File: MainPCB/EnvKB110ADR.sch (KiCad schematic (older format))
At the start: 246 parts, among them U1 MCP23017, U2 Pico

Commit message: setup some board bits
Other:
- moved on the sheet: D_0, D_1, D_10, D_100, D_101, D_102, D_103, D_104, D_105, D_106, D_107, D_108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

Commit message: Started work on swapping RPI pico for STM32F411CEU6
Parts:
- removed D_0, D_1, D_10, D_11, D_2, D_3, D_4, D_5, D_6, D_7, D_8, D_9: SOD-123, Diode_SMD:D_SOD-123, symbol Device:D_Small
- removed H7: MountingHole, MountingHole:MountingHole_2.2mm_M2, symbol Mechanical:MountingHole
- removed K_0, K_1, K_10, K_11, K_2, K_3, K_4, K_5, K_6, K_7, K_8, K_9: KEYSW, MX_Only:MXOnly-1U-Hotswap, symbol MX_Alps_Hybrid:MX-NoLED
- removed U1: MCP23017, Package_SO:SOIC-28W_7.5x17.9mm_P1.27mm, symbol Interface_Expansion:MCP23017_SO
- removed U2: Pico, MCU_RaspberryPi_and_Boards:RPi_Pico_SMD_TH, symbol MCU_RaspberryPi_and_Boards:Pico
- added C1, C2, C3, C4: 100nf capacitor, Capacitor_SMD:C_0402_1005Metric, symbol Device:C_Small
- added R1: 1.5K, Resistor_SMD:R_0402_1005Metric, symbol Device:R_Small
- added R2, R5: 5.1K 0402, Resistor_SMD:R_0402_1005Metric, symbol Device:R_Small
- added R3, R4: 22ohm, Resistor_SMD:R_0402_1005Metric, symbol Device:R_Small
- added U1: XC6206PxxxMR, Package_TO_SOT_SMD:SOT-23, symbol Regulator_Linear:XC6206PxxxMR
- added U2: STM32F411CEUx, Package_DFN_QFN:QFN-48-1EP_7x7mm_P0.5mm_EP5.6x5.6mm, symbol MCU_ST_STM32F4:STM32F411CEUx
- added USB1: HRO-TYPE-C-31-M-12, Type-C:HRO-TYPE-C-31-M-12-Assembly, symbol Type-C:HRO-TYPE-C-31-M-12
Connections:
- net labels added: D+, D-, PA11, PA12, VBUS
- net labels removed: SCL, SDA, col18, row0
- wire segments 468 -> 445
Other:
- note added: "these capacitors should all be placed\n near the power pin of the STM32"
- note added: "unsure what this pullup resistor is for\nbut its used in some MCU boards so lets copy it"

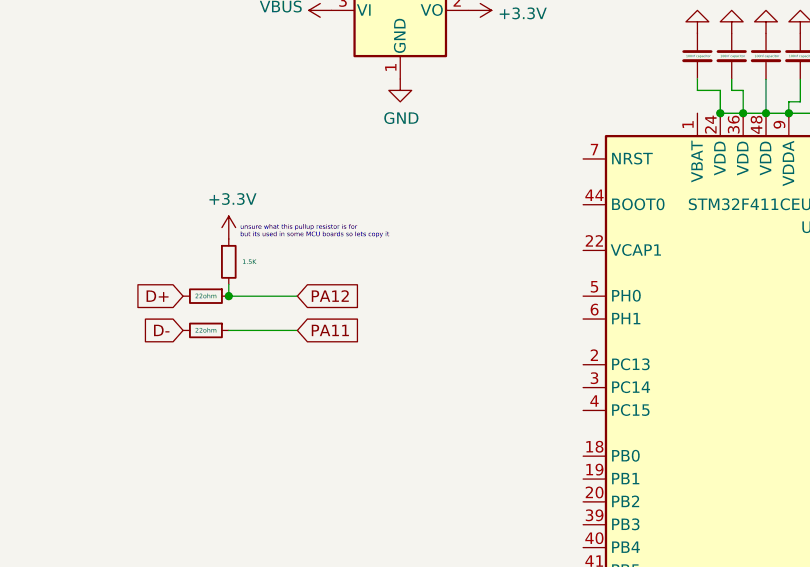
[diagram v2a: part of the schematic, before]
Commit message: added some notes in the schematic
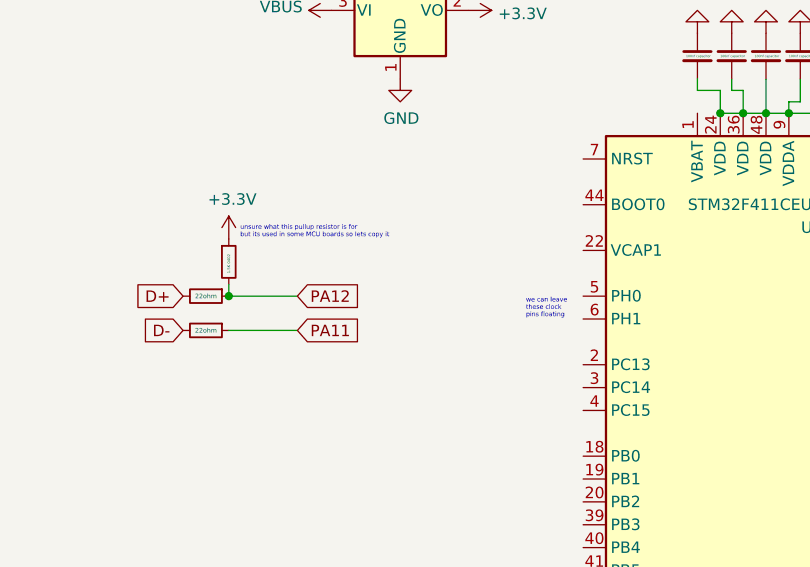
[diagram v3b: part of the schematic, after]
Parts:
- R1: value 1.5K -> 1.5K 0402
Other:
- note added: "we can leave \nthese clock\npins floating"
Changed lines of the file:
@@
 P 11150 10500
 F 0 "R1" H 11209 10546 50  0001 L CNN
-F 1 "1.5K" H 11209 10500 20  0000 L CNN
+F 1 "1.5K 0402" V 11150 10450 12  0000 L CNN
 F 2 "Resistor_SMD:R_0402_1005Metric" H 11150 10500 50  0001 C CNN
 F 3 "~" H 11150 10500 50  0001 C CNN
@@
 	1    0    0    -1
 $EndComp
+Text Notes 12450 10750 0    20   ~ 0
+we can leave \nthese clock\npins floating
 $EndSCHEMATC

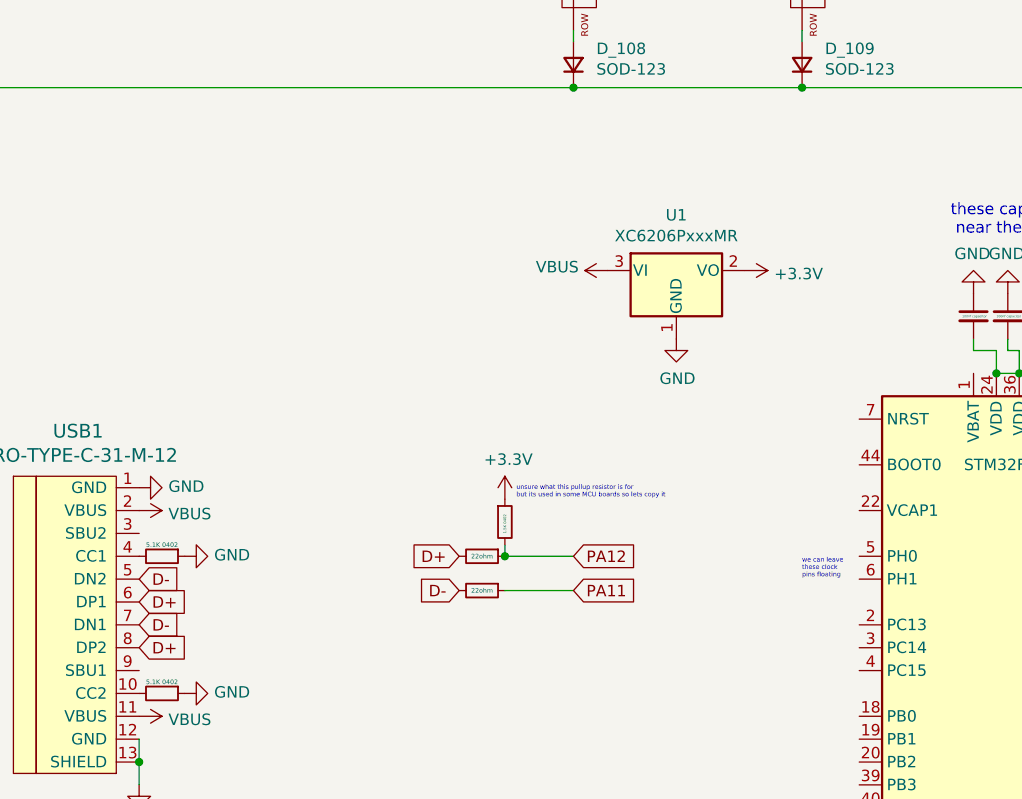
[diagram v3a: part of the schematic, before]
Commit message: hopefully correct implementation of a 8mhz oscilator
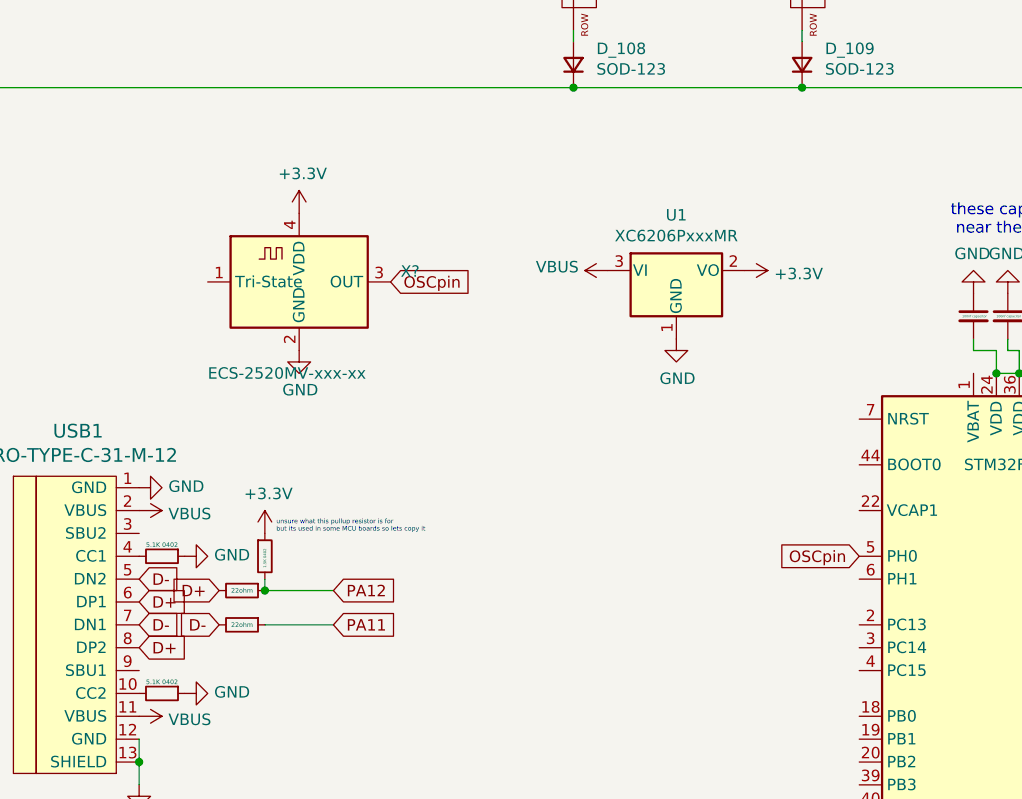
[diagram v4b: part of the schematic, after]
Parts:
- added X?: ECS-2520MV-xxx-xx, Oscillator:Oscillator_SMD_ECS_2520MV-xxx-xx-4Pin_2.5x2.0mm, symbol Oscillator:ECS-2520MV-xxx-xx
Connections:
- net +3V3: now also X?.4 (VDD)
- net GND: now also X?.2 (GND)
- net OSCpin: now reaches U2.5 (PH0)
- net OSCpin: now also X?.3 (OUT)
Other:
- note removed: "we can leave \nthese clock\npins floating"
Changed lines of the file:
@@
 Text GLabel 9550 11050 2    50   Input ~ 0
 D+
-Text GLabel 10950 10650 0    50   Input ~ 0
+Text GLabel 9900 10800 0    50   Input ~ 0
 D+
-Text GLabel 10950 10800 0    50   Input ~ 0
+Text GLabel 9900 10950 0    50   Input ~ 0
 D-
 $Comp
 L Device:R_Small R3
 U 1 1 6149657B
-P 11050 10650
-F 0 "R3" V 10854 10650 50  0001 C CNN
-F 1 "22ohm" V 11050 10650 20  0000 C CNN
-F 2 "Resistor_SMD:R_0402_1005Metric" H 11050 10650 50  0001 C CNN
-F 3 "~" H 11050 10650 50  0001 C CNN
-	1    11050 10650
+P 10000 10800
+F 0 "R3" V 9804 10800 50  0001 C CNN
+F 1 "22ohm" V 10000 10800 20  0000 C CNN
+F 2 "Resistor_SMD:R_0402_1005Metric" H 10000 10800 50  0001 C CNN
+F 3 "~" H 10000 10800 50  0001 C CNN
+	1    10000 10800
 	0    1    1    0
 $EndComp
@@
 L Device:R_Small R4
 U 1 1 614993EB
-P 11050 10800
-F 0 "R4" V 10854 10800 50  0001 C CNN
-F 1 "22ohm" V 11050 10800 20  0000 C CNN
-F 2 "Resistor_SMD:R_0402_1005Metric" H 11050 10800 50  0001 C CNN
-F 3 "~" H 11050 10800 50  0001 C CNN
-	1    11050 10800
+P 10000 10950
+F 0 "R4" V 9804 10950 50  0001 C CNN
+F 1 "22ohm" V 10000 10950 20  0000 C CNN
+F 2 "Resistor_SMD:R_0402_1005Metric" H 10000 10950 50  0001 C CNN
+F 3 "~" H 10000 10950 50  0001 C CNN
+	1    10000 10950
 	0    1    1    0
 $EndComp
@@
 L power:+3.3V #PWR0110
 U 1 1 6149994E
-P 11150 10400
-F 0 "#PWR0110" H 11150 10250 50  0001 C CNN
-F 1 "+3.3V" H 11165 10573 50  0000 C CNN
-F 2 "" H 11150 10400 50  0001 C CNN
-F 3 "" H 11150 10400 50  0001 C CNN
-	1    11150 10400
+P 10100 10550
+F 0 "#PWR0110" H 10100 10400 50  0001 C CNN
+F 1 "+3.3V" H 10115 10723 50  0000 C CNN
+F 2 "" H 10100 10550 50  0001 C CNN
+F 3 "" H 10100 10550 50  0001 C CNN
+	1    10100 10550
 	1    0    0    -1
 $EndComp
@@
 L Device:R_Small R1
 U 1 1 6149AD81
-P 11150 10500
-F 0 "R1" H 11209 10546 50  0001 L CNN
-F 1 "1.5K 0402" V 11150 10450 12  0000 L CNN
-F 2 "Resistor_SMD:R_0402_1005Metric" H 11150 10500 50  0001 C CNN
-F 3 "~" H 11150 10500 50  0001 C CNN
-	1    11150 10500
+P 10100 10650
+F 0 "R1" H 10159 10696 50  0001 L CNN
+F 1 "1.5K 0402" V 10100 10600 12  0000 L CNN
+F 2 "Resistor_SMD:R_0402_1005Metric" H 10100 10650 50  0001 C CNN
+F 3 "~" H 10100 10650 50  0001 C CNN
+	1    10100 10650
 	1    0    0    -1
 $EndComp
 Wire Wire Line
-	11150 10600 11150 10650
+	10100 10750 10100 10800
 Wire Wire Line
-	11150 10650 11450 10650
-Connection ~ 11150 10650
+	10100 10800 10400 10800
+Connection ~ 10100 10800
 Wire Wire Line
-	11150 10800 11450 10800
-Text GLabel 11450 10650 2    50   Input ~ 0
+	10100 10950 10400 10950
+Text GLabel 10400 10800 2    50   Input ~ 0
 PA12
-Text GLabel 11450 10800 2    50   Input ~ 0
+Text GLabel 10400 10950 2    50   Input ~ 0
 PA11
 Text GLabel 14000 12450 2    50   Input ~ 0
@@
 Text GLabel 14000 12350 2    50   Input ~ 0
 PA11
-Text Notes 11200 10400 0    20   ~ 0
+Text Notes 10150 10550 0    20   ~ 0
 unsure what this pullup resistor is for\nbut its used in some MCU boards so lets copy it
 $Comp
@@
 	1    0    0    -1
 $EndComp
-Text Notes 12450 10750 0    20   ~ 0
-we can leave \nthese clock\npins floating
+$Comp
+L Oscillator:ECS-2520MV-xxx-xx X?
+U 1 1 60E5B405
+P 10250 9450
+F 0 "X?" H 10694 9496 50  0000 L CNN
+F 1 "ECS-2520MV-xxx-xx" H 9850 9050 50  0000 L CNN
+F 2 "Oscillator:Oscillator_SMD_ECS_2520MV-xxx-xx-4Pin_2.5x2.0mm" H 10700 9100 50  0001 C CNN
+F 3 "https://www.ecsxtal.com/store/pdf/ECS-2520MV.pdf" H 10075 9575 50  0001 C CNN
+	1    10250 9450
+	1    0    0    -1
+$EndComp
+Text GLabel 10650 9450 2    50   Input ~ 0
+OSCpin
+Text GLabel 12700 10650 0    50   Input ~ 0
+OSCpin
+$Comp
+L power:+3.3V #PWR?
+U 1 1 60E980B3
+P 10250 9150
+F 0 "#PWR?" H 10250 9000 50  0001 C CNN
+F 1 "+3.3V" H 10265 9323 50  0000 C CNN
+F 2 "" H 10250 9150 50  0001 C CNN
+F 3 "" H 10250 9150 50  0001 C CNN
+	1    10250 9150
+	1    0    0    -1
+$EndComp
+$Comp
+L power:GND #PWR?
+U 1 1 60E99EB6
+P 10250 9750
+F 0 "#PWR?" H 10250 9500 50  0001 C CNN
+F 1 "GND" H 10255 9577 50  0000 C CNN
+F 2 "" H 10250 9750 50  0001 C CNN
+F 3 "" H 10250 9750 50  0001 C CNN
+	1    10250 9750
+	1    0    0    -1
+$EndComp
 $EndSCHEMATC

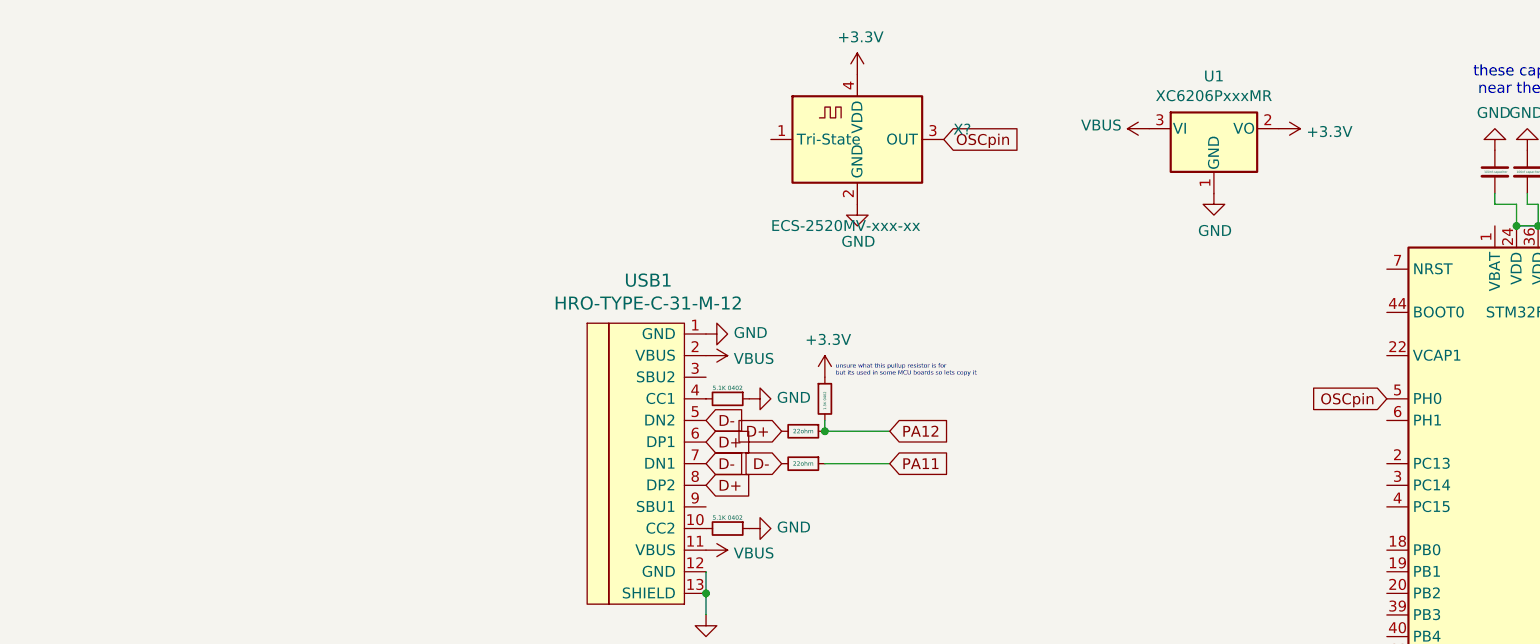
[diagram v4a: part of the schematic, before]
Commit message: added boot and reset switches
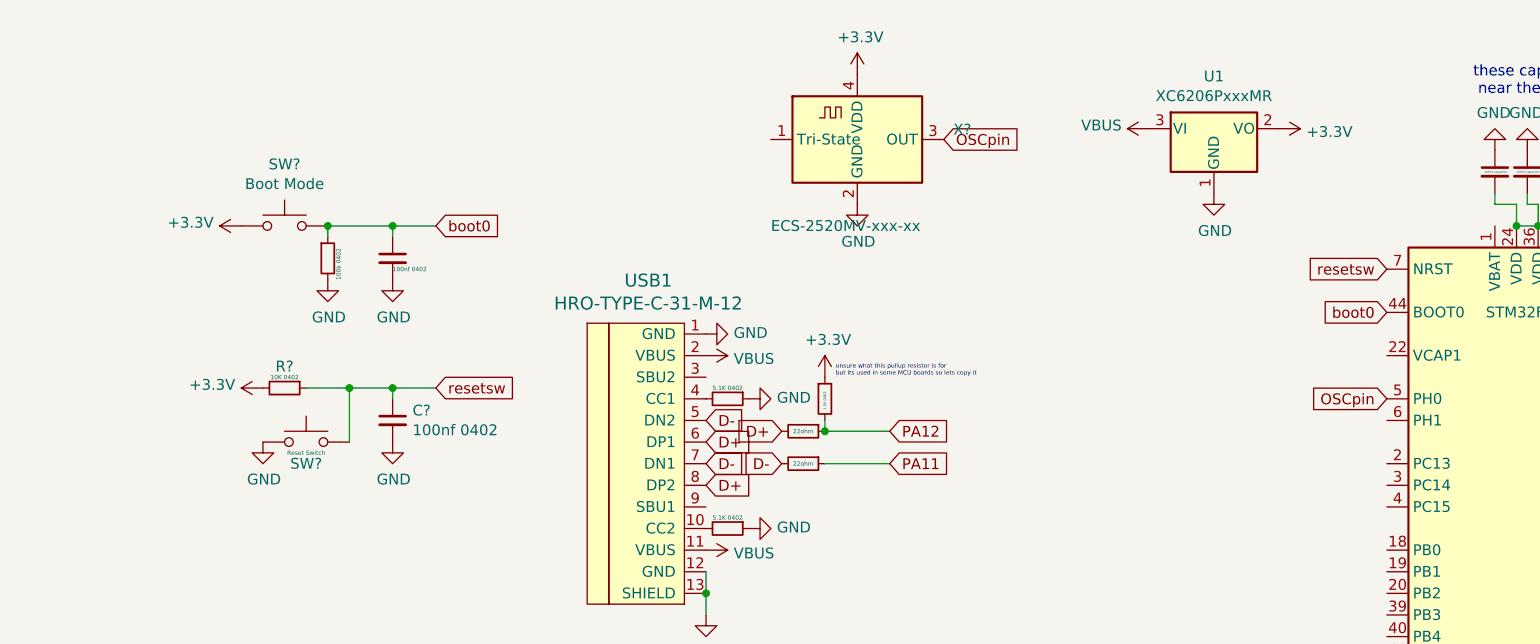
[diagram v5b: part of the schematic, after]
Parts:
- added C? (x2): 100nf 0402, Capacitor_SMD:C_0402_1005Metric, symbol Device:C_Small
- added R?: 100k 0402, Resistor_SMD:R_0402_1005Metric, symbol Device:R_Small
- added R?: 10K 0402, Resistor_SMD:R_0402_1005Metric, symbol Device:R_Small
- added SW?: Boot Mode, Button_Switch_SMD:SW_DIP_SPSTx01_Slide_6.7x4.1mm_W6.73mm_P2.54mm_LowProfile_JPin, symbol Switch:SW_Push
- added SW?: Reset Switch, Button_Switch_SMD:SW_DIP_SPSTx01_Slide_6.7x4.1mm_W6.73mm_P2.54mm_LowProfile_JPin, symbol Switch:SW_Push
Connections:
- net +3V3: now also R?.2, SW?.1
- net GND: now also C?.2, C?.2, R?.2, SW?.1
- net boot0: now reaches U2.44 (BOOT0)
- net boot0: now also C?.1, R?.1, SW?.2
- net resetsw: now reaches U2.7 (NRST)
- net resetsw: now also C?.1, R?.1, SW?.2
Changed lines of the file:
@@
 	1    0    0    -1
 $EndComp
+Text GLabel 12700 10250 0    50   Input ~ 0
+boot0
+Text GLabel 8300 9850 2    50   Input ~ 0
+boot0
+$Comp
+L power:GND #PWR?
+U 1 1 60E6F770
+P 8100 10100
+F 0 "#PWR?" H 8100 9850 50  0001 C CNN
+F 1 "GND" H 8105 9927 50  0000 C CNN
+F 2 "" H 8100 10100 50  0001 C CNN
+F 3 "" H 8100 10100 50  0001 C CNN
+	1    8100 10100
+	1    0    0    -1
+$EndComp
+$Comp
+L power:GND #PWR?
+U 1 1 60E6FF51
+P 7800 10100
+F 0 "#PWR?" H 7800 9850 50  0001 C CNN
+F 1 "GND" H 7805 9927 50  0000 C CNN
+F 2 "" H 7800 10100 50  0001 C CNN
+F 3 "" H 7800 10100 50  0001 C CNN
+	1    7800 10100
+	1    0    0    -1
+$EndComp
+$Comp
+L Device:R_Small R?
+U 1 1 60E71B24
+P 7800 10000
+F 0 "R?" H 7859 10046 50  0001 L CNN
+F 1 "100k 0402" V 7850 9900 20  0000 L CNN
+F 2 "Resistor_SMD:R_0402_1005Metric" H 7800 10000 50  0001 C CNN
+F 3 "~" H 7800 10000 50  0001 C CNN
+	1    7800 10000
+	1    0    0    -1
+$EndComp
+$Comp
+L Device:C_Small C?
+U 1 1 60E73582
+P 8100 10000
+F 0 "C?" H 8192 10046 50  0001 L CNN
+F 1 "100nf 0402" H 8100 9950 20  0000 L CNN
+F 2 "Capacitor_SMD:C_0402_1005Metric" H 8100 10000 50  0001 C CNN
+F 3 "~" H 8100 10000 50  0001 C CNN
+	1    8100 10000
+	1    0    0    -1
+$EndComp
+Wire Wire Line
+	8300 9850 8100 9850
+Wire Wire Line
+	8100 9850 8100 9900
+Wire Wire Line
+	8100 9850 7800 9850
+Wire Wire Line
+	7800 9850 7800 9900
+Connection ~ 8100 9850
+$Comp
+L Switch:SW_Push SW?
+U 1 1 60EE310E
+P 7600 9850
+F 0 "SW?" H 7600 10135 50  0000 C CNN
+F 1 "Boot Mode" H 7600 10044 50  0000 C CNN
+F 2 "Button_Switch_SMD:SW_DIP_SPSTx01_Slide_6.7x4.1mm_W6.73mm_P2.54mm_LowProfile_JPin" H 7600 10043 50  0001 C CNN
+F 3 "~" H 7600 10050 50  0001 C CNN
+	1    7600 9850
+	1    0    0    -1
+$EndComp
+Connection ~ 7800 9850
+$Comp
+L power:+3.3V #PWR?
+U 1 1 60EE5DF1
+P 7400 9850
+F 0 "#PWR?" H 7400 9700 50  0001 C CNN
+F 1 "+3.3V" V 7415 9978 50  0000 L CNN
+F 2 "" H 7400 9850 50  0001 C CNN
+F 3 "" H 7400 9850 50  0001 C CNN
+	1    7400 9850
+	0    -1   -1   0
+$EndComp
+Text GLabel 12700 10050 0    50   Input ~ 0
+resetsw
+Text GLabel 8300 10600 2    50   Input ~ 0
+resetsw
+$Comp
+L power:GND #PWR?
+U 1 1 60EED52E
+P 8100 10850
+F 0 "#PWR?" H 8100 10600 50  0001 C CNN
+F 1 "GND" H 8105 10677 50  0000 C CNN
+F 2 "" H 8100 10850 50  0001 C CNN
+F 3 "" H 8100 10850 50  0001 C CNN
+	1    8100 10850
+	1    0    0    -1
+$EndComp
+$Comp
+L power:GND #PWR?
+U 1 1 60EEEB39
+P 7500 10850
+F 0 "#PWR?" H 7500 10600 50  0001 C CNN
+F 1 "GND" H 7505 10677 50  0000 C CNN
+F 2 "" H 7500 10850 50  0001 C CNN
+F 3 "" H 7500 10850 50  0001 C CNN
+	1    7500 10850
+	1    0    0    -1
+$EndComp
+$Comp
+L Device:C_Small C?
+U 1 1 60EEF344
+P 8100 10750
+F 0 "C?" H 8192 10796 50  0000 L CNN
+F 1 "100nf 0402" H 8192 10705 50  0000 L CNN
+F 2 "Capacitor_SMD:C_0402_1005Metric" H 8100 10750 50  0001 C CNN
+F 3 "~" H 8100 10750 50  0001 C CNN
+	1    8100 10750
+	1    0    0    -1
+$EndComp
+$Comp
+L Device:R_Small R?
+U 1 1 60EF0D18
+P 7600 10600
+F 0 "R?" V 7500 10600 50  0000 C CNN
+F 1 "10K 0402" V 7550 10600 20  0000 C CNN
+F 2 "Resistor_SMD:R_0402_1005Metric" H 7600 10600 50  0001 C CNN
+F 3 "~" H 7600 10600 50  0001 C CNN
+	1    7600 10600
+	0    1    1    0
+$EndComp
+$Comp
+L power:+3.3V #PWR?
+U 1 1 60EF228D
+P 7500 10600
+F 0 "#PWR?" H 7500 10450 50  0001 C CNN
+F 1 "+3.3V" V 7515 10728 50  0000 L CNN
+F 2 "" H 7500 10600 50  0001 C CNN
+F 3 "" H 7500 10600 50  0001 C CNN
+	1    7500 10600
+	0    -1   -1   0
+$EndComp
+Wire Wire Line
+	8100 10650 8100 10600
+Wire Wire Line
+	8100 10600 8300 10600
+Wire Wire Line
+	8100 10600 7900 10600
+Connection ~ 8100 10600
+$Comp
+L Switch:SW_Push SW?
+U 1 1 60F65F42
+P 7700 10850
+F 0 "SW?" H 7700 10750 50  0000 C CNN
+F 1 "Reset Switch" H 7700 10800 20  0000 C CNN
+F 2 "Button_Switch_SMD:SW_DIP_SPSTx01_Slide_6.7x4.1mm_W6.73mm_P2.54mm_LowProfile_JPin" H 7700 11043 50  0001 C CNN
+F 3 "~" H 7700 11050 50  0001 C CNN
+	1    7700 10850
+	1    0    0    -1
+$EndComp
+Wire Wire Line
+	7900 10850 7900 10600
+Connection ~ 7900 10600
+Wire Wire Line
+	7900 10600 7700 10600
 $EndSCHEMATC
